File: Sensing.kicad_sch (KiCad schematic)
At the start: 7 parts

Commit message: fix: bom improvements & more notes
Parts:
- TP301: footprint TestPoint:TestPoint_THTPad_2.0x2.0mm_Drill1.0mm -> RD-Testpoints:TestPoint_THTPad_1.5x1.5mm_Drill0.7mm
- TP302, TP303: footprint TestPoint:TestPoint_Pad_D1.5mm -> RD-Testpoints:TestPoint_Pad_D1.5mm
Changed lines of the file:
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@@
 			)
 		)
-		(property "Footprint" "TestPoint:TestPoint_Pad_D1.5mm"
+		(property "Footprint" "RD-Testpoints:TestPoint_Pad_D1.5mm"
 			(at 177.8 74.93 0)
 			(effects
@@
 			)
 		)
-		(property "Footprint" "TestPoint:TestPoint_Pad_D1.5mm"
+		(property "Footprint" "RD-Testpoints:TestPoint_Pad_D1.5mm"
 			(at 148.59 74.93 0)
 			(effects
@@
 			)
 		)
-		(property "Footprint" "TestPoint:TestPoint_THTPad_2.0x2.0mm_Drill1.0mm"
+		(property "Footprint" "RD-Testpoints:TestPoint_THTPad_1.5x1.5mm_Drill0.7mm"
 			(at 129.54 101.6 0)
 			(effects

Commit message: feat: ERC/DRC checks
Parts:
- R301, R302, R303, R304: Manufacturer (none) -> Analog Technologies
- TP301: now left out of the parts list

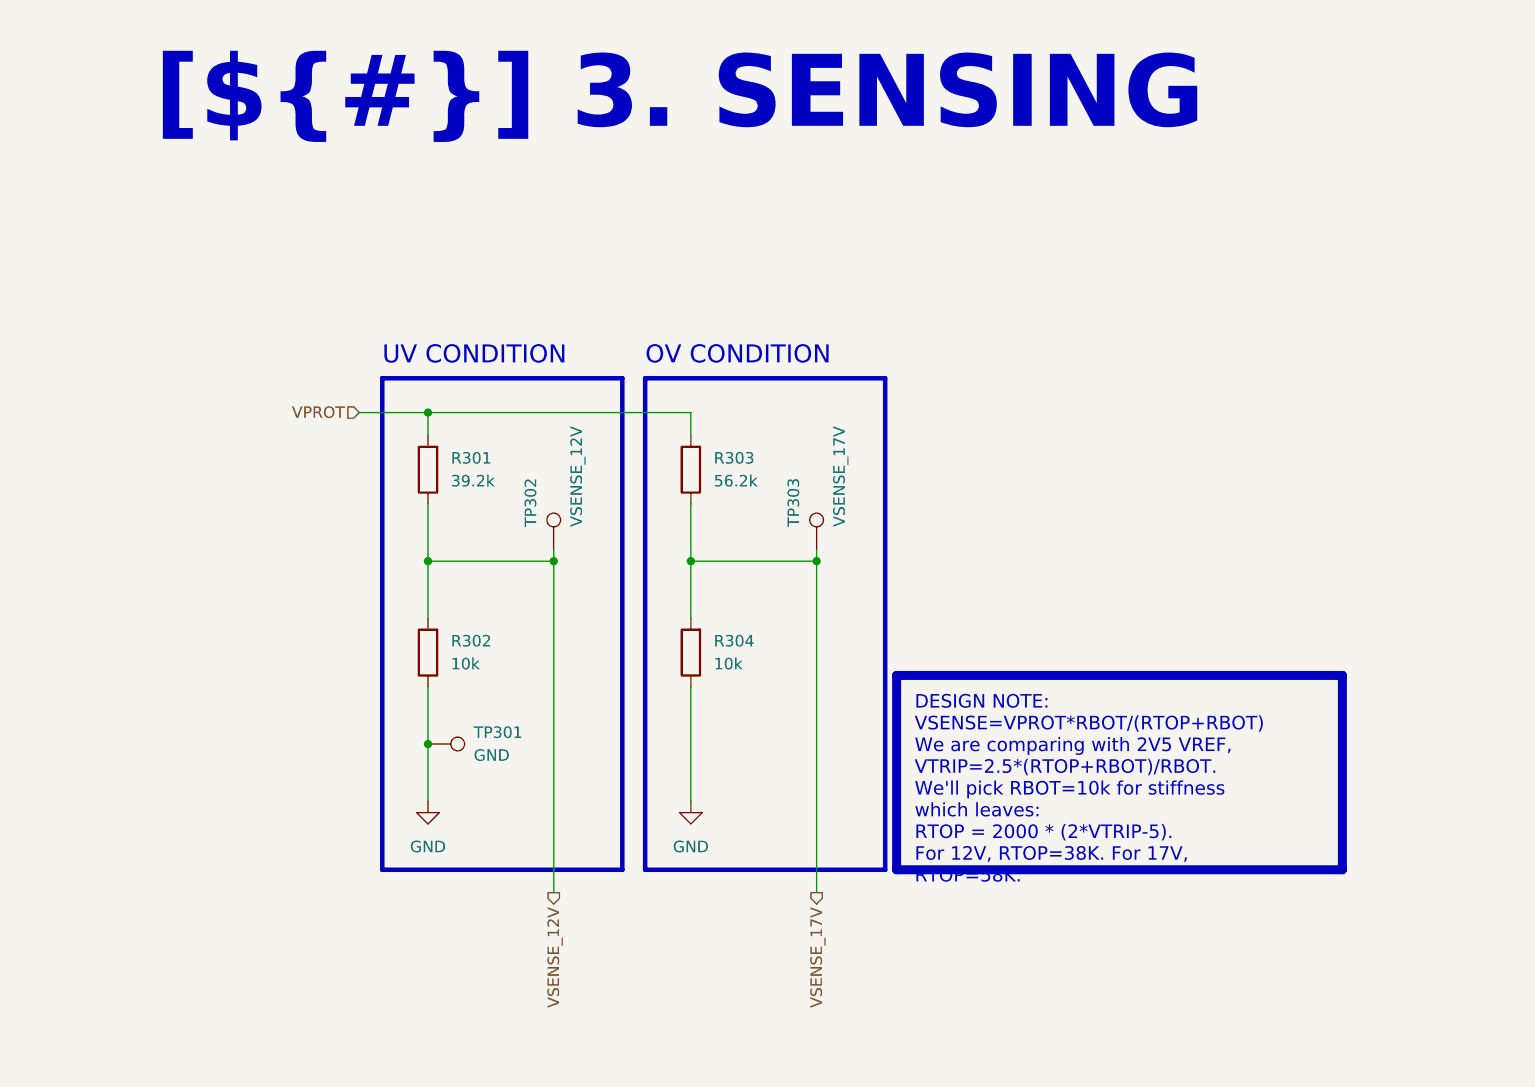
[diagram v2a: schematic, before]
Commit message: feat!: added OC protection, redesigned board from near scratch, size increase
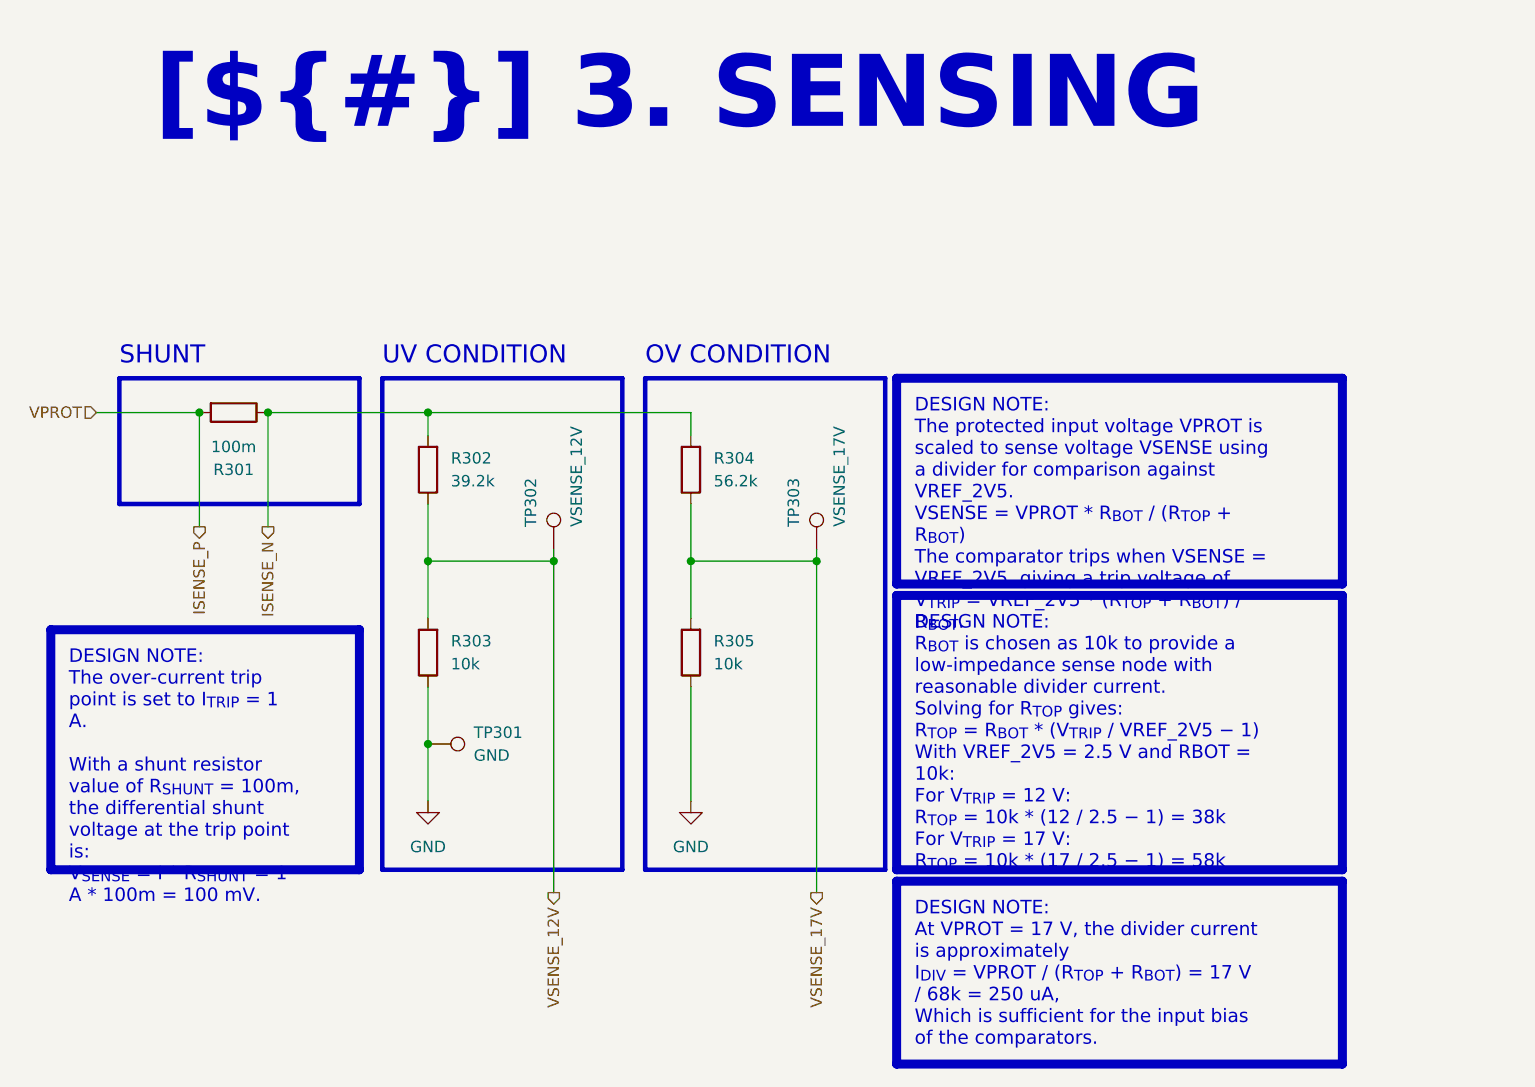
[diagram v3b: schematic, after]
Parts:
- added R301: 100m, Resistor_SMD:R_1206_3216Metric_Pad1.30x1.75mm_HandSolder, symbol Device:R
- TP302, TP303: footprint RD-Testpoints:TestPoint_Pad_D1.5mm -> RD-Testpoints:TestPoint_Pad_D1.0mm
- renumbered R301 to R302, R302 to R303, R303 to R304, R304 to R305
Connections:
- net VPROT renamed ISENSE_N
- net ISENSE_N: now also R301.1
- new net ISENSE_P: R301.2
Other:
- note added: "SHUNT"

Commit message: feat: revision A release
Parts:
- R301: MPN (none) -> KDV12FR100ET; Manufacturer Part Number KDV12FR100ET -> (none)
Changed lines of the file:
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@@
 			)
 		)
-		(property "Manufacturer Part Number" "KDV12FR100ET"
+		(property "Manufacturer Part Number" ""
 			(at 107.95 59.69 0)
 			(effects
@@
 			(at 107.95 59.69 90)
 			(effects
+				(font
+					(size 1.27 1.27)
+				)
+				(hide yes)
+			)
+		)
+		(property "MPN" "KDV12FR100ET"
+			(at 107.95 59.69 90)
+			(effects
